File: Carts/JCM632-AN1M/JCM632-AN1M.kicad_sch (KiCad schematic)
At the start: 16 parts, among them IC1 uPD23C16000WGX, IC2 HM9264LF15, J1 Loopy-Cart-Edge

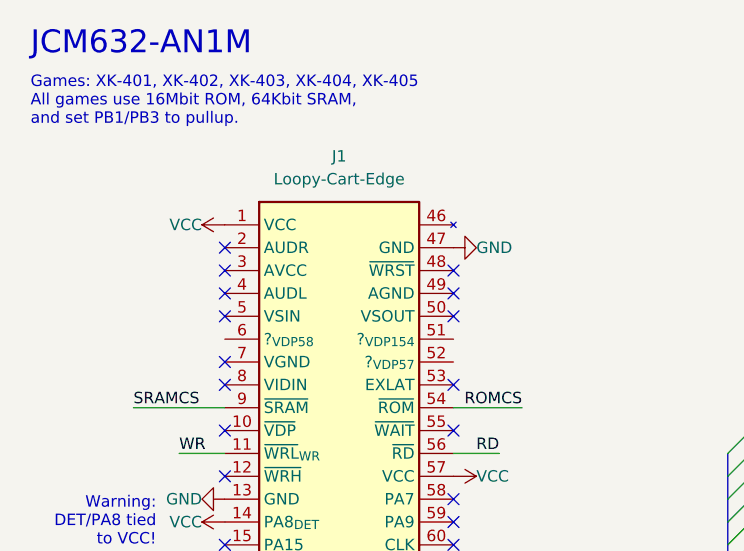
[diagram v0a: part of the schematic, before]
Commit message: Unify project part libs
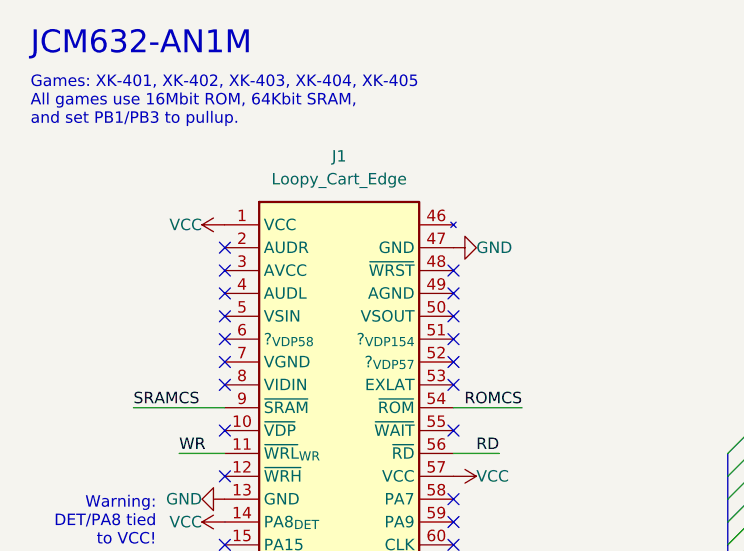
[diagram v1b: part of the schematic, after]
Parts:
- IC1: symbol project-parts:ROM_16Mbit_SOP44_Physical -> loopy-parts:ROM_16Mbit_SOP44_Physical
- IC2: symbol project-parts:SRAM_64Kbit_SOP28_Physical -> loopy-parts:SRAM_64Kbit_SOP28_Physical
- J1: value Loopy-Cart-Edge -> Loopy_Cart_Edge; footprint project-parts:Loopy-Cart-Edge -> loopy-parts:Loopy_Cart_Edge; symbol project-parts:Loopy-Cart-Edge -> loopy-parts:Loopy_Cart_Edge
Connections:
- no-connect marks 33 -> 36
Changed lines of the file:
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@@
 	)
 	(no_connect
+		(at 60.96 48.26)
+	)
+	(no_connect
 		(at 35.56 81.28)
 	)
 	(no_connect
+		(at 60.96 50.8)
+	)
+	(no_connect
 		(at 35.56 53.34)
 	)
 	(no_connect
+		(at 35.56 48.26)
+	)
+	(no_connect
 		(at 35.56 71.12)
 	)
@@
 	)
 	(symbol
-		(lib_id "project-parts:ROM_16Mbit_SOP44_Physical")
+		(lib_id "loopy-parts:ROM_16Mbit_SOP44_Physical")
 		(at 127 49.53 0)
 		(unit 1)
@@
 	)
 	(symbol
-		(lib_id "project-parts:SRAM_64Kbit_SOP28_Physical")
+		(lib_id "loopy-parts:SRAM_64Kbit_SOP28_Physical")
 		(at 200.66 39.37 0)
 		(unit 1)
@@
 	)
 	(symbol
-		(lib_id "project-parts:Loopy-Cart-Edge")
+		(lib_id "loopy-parts:Loopy_Cart_Edge")
 		(at 48.26 91.44 0)
 		(unit 1)
@@
 			)
 		)
-		(property "Value" "Loopy-Cart-Edge"
+		(property "Value" "Loopy_Cart_Edge"
 			(at 48.26 30.48 0)
 			(effects
@@
 			)
 		)
-		(property "Footprint" "project-parts:Loopy-Cart-Edge"
+		(property "Footprint" "loopy-parts:Loopy_Cart_Edge"
 			(at 48.26 33.02 0)
 			(effects
